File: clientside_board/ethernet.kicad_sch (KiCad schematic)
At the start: 20 parts, among them J3 Ethernet Jack, U2 ENC624J600-I_PT, Y1 25MHz parallel resonant

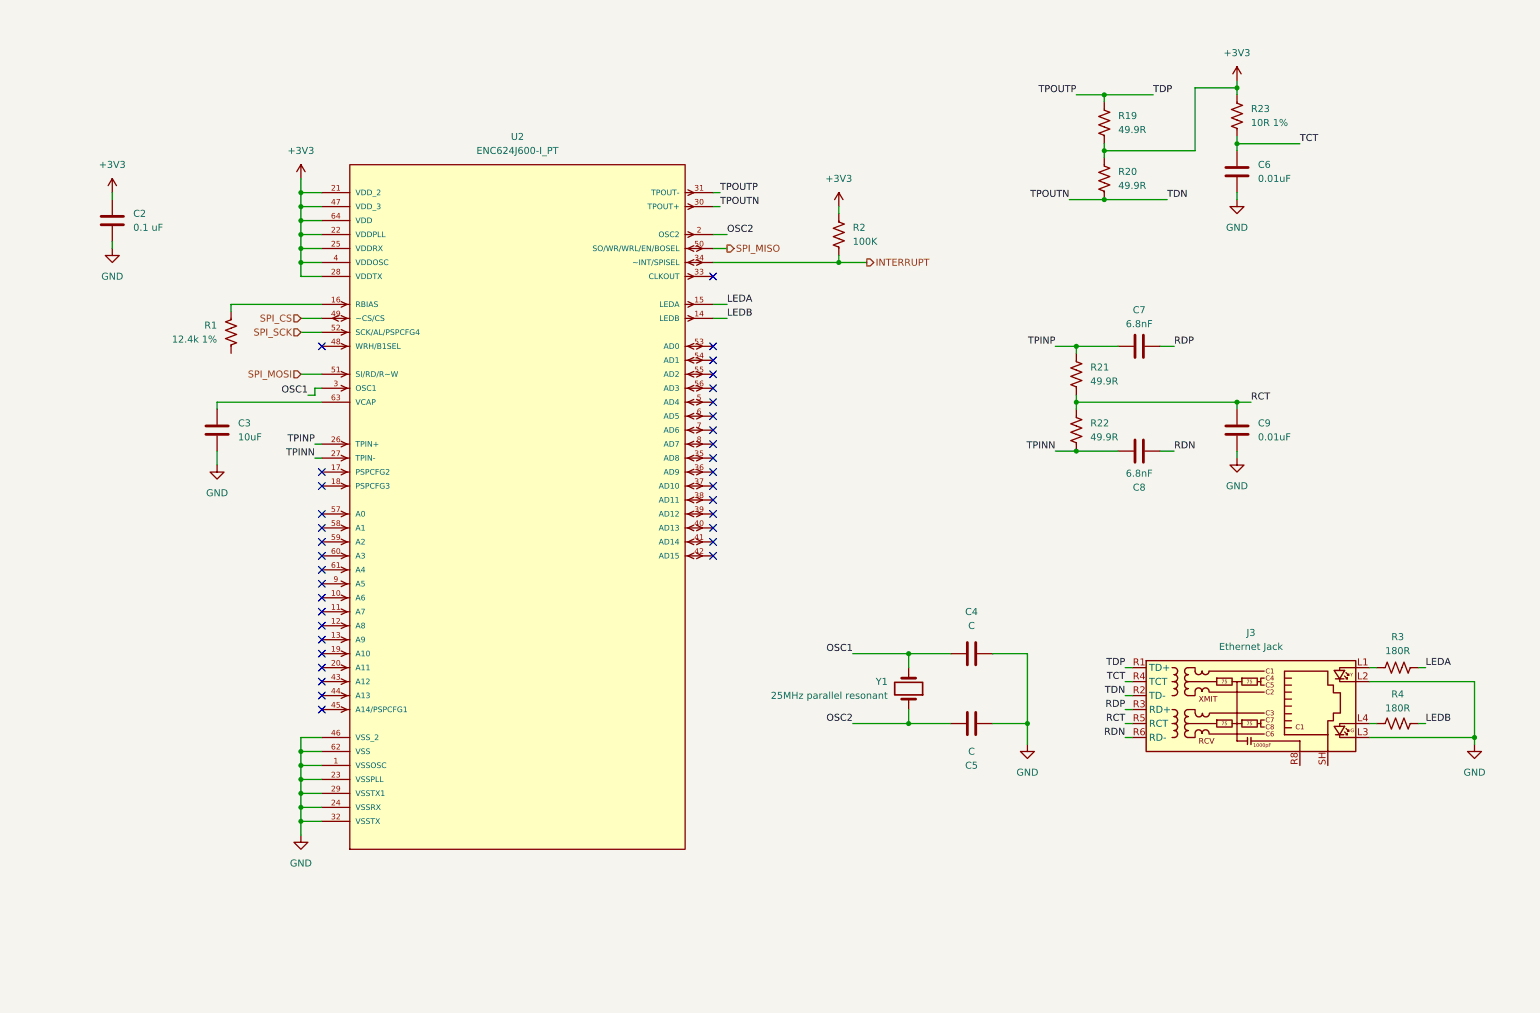
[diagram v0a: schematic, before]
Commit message: Cleanup Power and Ethernet Sheet
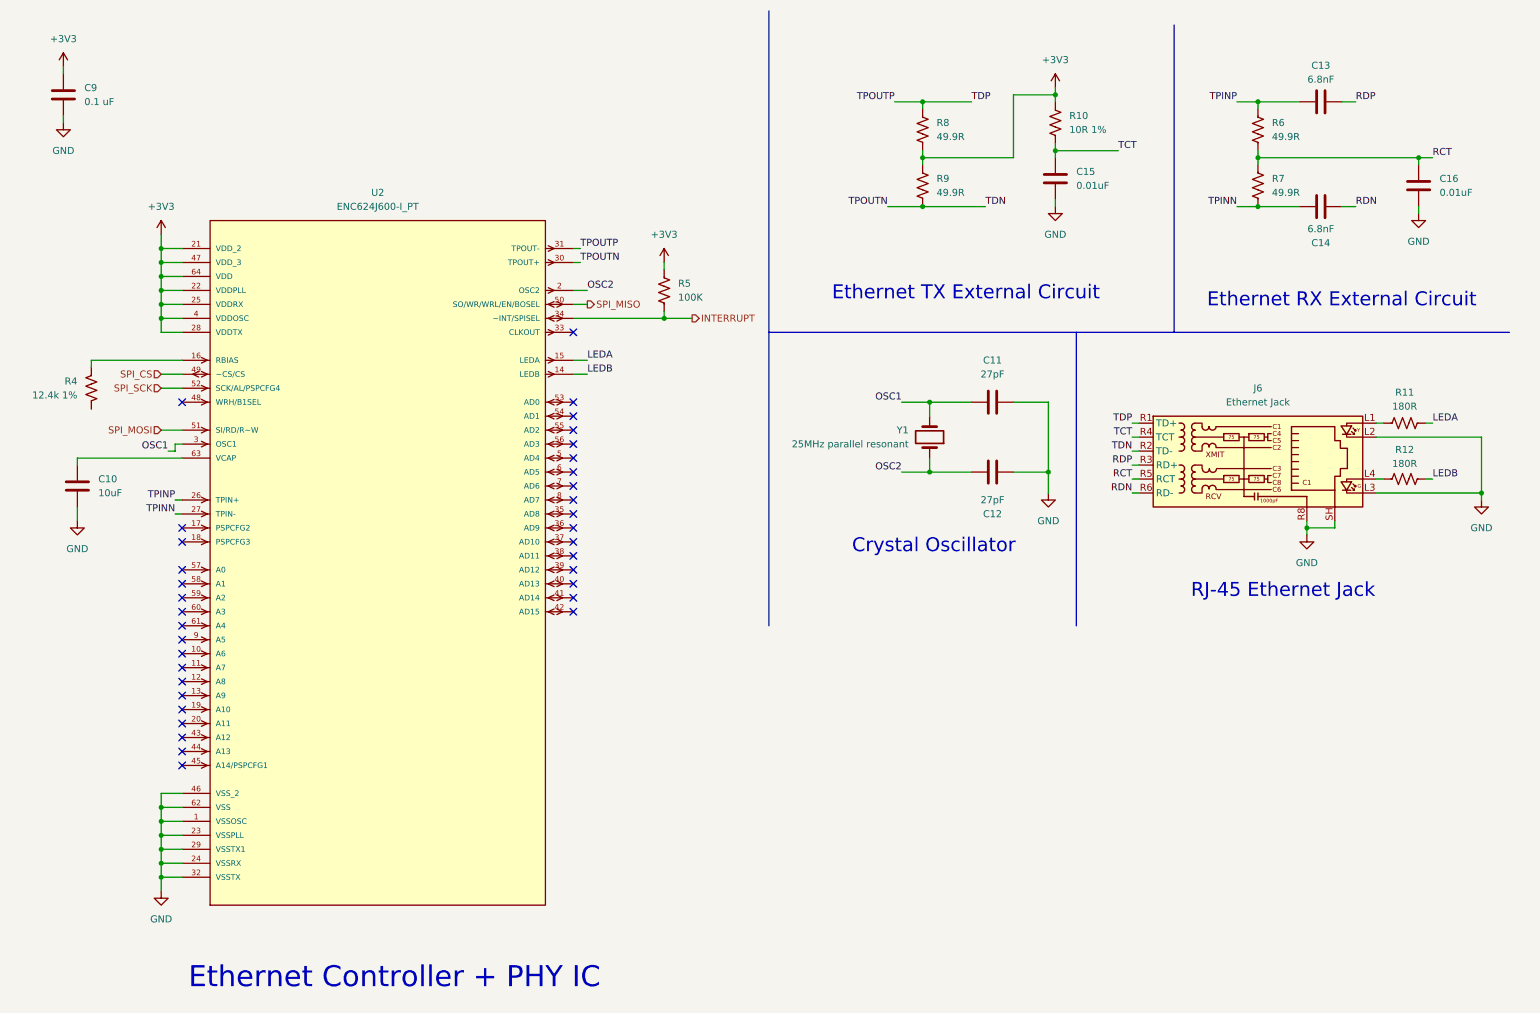
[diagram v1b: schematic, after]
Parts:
- C10: renamed from C3; footprint (none) -> Capacitor_SMD:C_0805_2012Metric_Pad1.18x1.45mm_HandSolder
- C11: renamed from C4; value C -> 27pF; footprint (none) -> Capacitor_SMD:C_0805_2012Metric_Pad1.18x1.45mm_HandSolder
- C12: renamed from C5; value C -> 27pF; footprint (none) -> Capacitor_SMD:C_0805_2012Metric_Pad1.18x1.45mm_HandSolder
- C13: renamed from C7; footprint (none) -> Capacitor_SMD:C_0805_2012Metric_Pad1.18x1.45mm_HandSolder
- C14: renamed from C8; footprint (none) -> Capacitor_SMD:C_0805_2012Metric_Pad1.18x1.45mm_HandSolder
- C15: renamed from C6; footprint (none) -> Capacitor_SMD:C_0805_2012Metric_Pad1.18x1.45mm_HandSolder
- C16: renamed from C9; footprint (none) -> Capacitor_SMD:C_0805_2012Metric_Pad1.18x1.45mm_HandSolder
- C9: renamed from C2; footprint (none) -> Capacitor_SMD:C_0805_2012Metric_Pad1.18x1.45mm_HandSolder
- renumbered J3 to J6, R23 to R10, R3 to R11, R4 to R12, R1 to R4, R2 to R5, R21 to R6, R22 to R7, R19 to R8, R20 to R9
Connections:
- net GND: now also J6.R8, J6.SH
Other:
- note added: "Crystal Oscillator"
- note added: "Ethernet Controller + PHY IC"
- note added: "Ethernet RX External Circuit"
- note added: "Ethernet TX External Circuit"
- note added: "RJ-45 Ethernet Jack"
- title: (none) -> Ethernet connection (Ethernet MAC+PHY and connector)
- moved on the sheet: C10, C11, C12, C13, C14, C15, C16, C9, J6, R10, R11, R12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

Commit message: Start MCU pin connection
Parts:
- renumbered C15 to C13, C13 to C14, C14 to C15, R7 to R10, R8 to R6, R9 to R7, R10 to R8, R6 to R9
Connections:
- net GND: now also R4.2
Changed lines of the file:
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@@
+	(wire
+		(pts
+			(xy 26.67 87.63) (xy 26.67 88.9)
+		)
+		(stroke
+			(width 0)
+			(type default)
+		)
+	)
 	(wire
 		(pts
@@
 		(dnp no)
 		(fields_autoplaced yes)
-		(property "Reference" "C15"
+		(property "Reference" "C13"
 			(at 205.74 44.4499 0)
 			(effects
@@
 			(project ""
 				(path "/94506b77-3097-414f-927c-35c0af27646f/c0b92ac7-0f0f-41de-974e-1086adc34351"
-					(reference "C15")
+					(reference "C13")
 					(unit 1)
 				)
@@
 		(dnp no)
 		(fields_autoplaced yes)
-		(property "Reference" "#PWR046"
+		(property "Reference" "#PWR047"
 			(at 279.4 110.49 0)
 			(effects
@@
 			(project ""
 				(path "/94506b77-3097-414f-927c-35c0af27646f/c0b92ac7-0f0f-41de-974e-1086adc34351"
-					(reference "#PWR046")
+					(reference "#PWR047")
 					(unit 1)
 				)
@@
 		(dnp no)
 		(fields_autoplaced yes)
-		(property "Reference" "#PWR0104"
+		(property "Reference" "#PWR045"
 			(at 247.65 116.84 0)
 			(effects
@@
 			(project ""
 				(path "/94506b77-3097-414f-927c-35c0af27646f/c0b92ac7-0f0f-41de-974e-1086adc34351"
-					(reference "#PWR0104")
+					(reference "#PWR045")
 					(unit 1)
 				)
@@
 		(dnp no)
 		(fields_autoplaced yes)
-		(property "Reference" "R10"
+		(property "Reference" "R8"
 			(at 204.47 34.2899 0)
 			(effects
@@
 			(project ""
 				(path "/94506b77-3097-414f-927c-35c0af27646f/c0b92ac7-0f0f-41de-974e-1086adc34351"
-					(reference "R10")
+					(reference "R8")
+					(unit 1)
+				)
+			)
+		)
+	)
+	(symbol
+		(lib_id "power:GND")
+		(at 26.67 88.9 0)
+		(unit 1)
+		(exclude_from_sim no)
+		(in_bom yes)
+		(on_board yes)
+		(dnp no)
+		(property "Reference" "#PWR0106"
+			(at 26.67 95.25 0)
+			(effects
+				(font
+					(size 1.27 1.27)
+				)
+				(hide yes)
+			)
+		)
+		(property "Value" "GND"
+			(at 26.67 93.218 0)
+			(effects
+				(font
+					(size 1.27 1.27)
+				)
+			)
+		)
+		(property "Footprint" ""
+			(at 26.67 88.9 0)
+			(effects
+				(font
+					(size 1.27 1.27)
+				)
+				(hide yes)
+			)
+		)
+		(property "Datasheet" ""
+			(at 26.67 88.9 0)
+			(effects
+				(font
+					(size 1.27 1.27)
+				)
+				(hide yes)
+			)
+		)
+		(property "Description" "Power symbol creates a global label with name \"GND\" , ground"
+			(at 26.67 88.9 0)
+			(effects
+				(font
+					(size 1.27 1.27)
+				)
+				(hide yes)
+			)
+		)
+		(pin "1"
+		)
+		(instances
+			(project ""
+				(path "/94506b77-3097-414f-927c-35c0af27646f/c0b92ac7-0f0f-41de-974e-1086adc34351"
+					(reference "#PWR0106")
 					(unit 1)
 				)
@@
 		(dnp no)
 		(fields_autoplaced yes)
-		(property "Reference" "R8"
+		(property "Reference" "R6"
 			(at 180.34 35.5599 0)
 			(effects
@@
 			(project ""
 				(path "/94506b77-3097-414f-927c-35c0af27646f/c0b92ac7-0f0f-41de-974e-1086adc34351"
-					(reference "R8")
+					(reference "R6")
 					(unit 1)
 				)
@@
 		(on_board yes)
 		(dnp no)
-		(property "Reference" "C14"
+		(property "Reference" "C15"
 			(at 250.19 57.404 90)
 			(effects
@@
 			(project "clientside_board"
 				(path "/94506b77-3097-414f-927c-35c0af27646f/c0b92ac7-0f0f-41de-974e-1086adc34351"
-					(reference "C14")
+					(reference "C15")
 					(unit 1)
 				)
@@
 		(dnp no)
 		(fields_autoplaced yes)
-		(property "Reference" "R6"
+		(property "Reference" "R9"
 			(at 241.3 35.5599 0)
 			(effects
@@
 			(project "clientside_board"
 				(path "/94506b77-3097-414f-927c-35c0af27646f/c0b92ac7-0f0f-41de-974e-1086adc34351"
-					(reference "R6")
+					(reference "R9")
 					(unit 1)
 				)
@@
 		(dnp no)
 		(fields_autoplaced yes)
-		(property "Reference" "#PWR045"
+		(property "Reference" "#PWR046"
 			(at 267.97 58.42 0)
 			(effects
@@
 			(project ""
 				(path "/94506b77-3097-414f-927c-35c0af27646f/c0b92ac7-0f0f-41de-974e-1086adc34351"
-					(reference "#PWR045")
+					(reference "#PWR046")
 					(unit 1)
 				)
@@
 		(on_board yes)
 		(dnp no)
-		(property "Reference" "C13"
+		(property "Reference" "C14"
 			(at 250.19 25.146 90)
 			(effects
@@
 			(project ""
 				(path "/94506b77-3097-414f-927c-35c0af27646f/c0b92ac7-0f0f-41de-974e-1086adc34351"
-					(reference "C13")
+					(reference "C14")
 					(unit 1)
 				)
@@
 		(dnp no)
 		(fields_autoplaced yes)
-		(property "Reference" "R7"
+		(property "Reference" "R10"
 			(at 241.3 45.7199 0)
 			(effects
@@
 			(project "clientside_board"
 				(path "/94506b77-3097-414f-927c-35c0af27646f/c0b92ac7-0f0f-41de-974e-1086adc34351"
-					(reference "R7")
+					(reference "R10")
 					(unit 1)
 				)
@@
 		(dnp no)
 		(fields_autoplaced yes)
-		(property "Reference" "R9"
+		(property "Reference" "R7"
 			(at 180.34 45.7199 0)
 			(effects
@@
 			(project "clientside_board"
 				(path "/94506b77-3097-414f-927c-35c0af27646f/c0b92ac7-0f0f-41de-974e-1086adc34351"
-					(reference "R9")
-					(unit 1)
-				)
+					(reference "R7")
+					(unit 1)
+				)

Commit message: Fix decoupling cap
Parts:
- removed Y1: 25MHz parallel resonant, symbol Device:Crystal
- added C13, C14, C15, C16: 0.1 uF, Capacitor_SMD:C_0805_2012Metric_Pad1.18x1.45mm_HandSolder, symbol Device:C
- added TP1: ETH_SPI_SCK, symbol Connector:TestPoint
- added TP2: ETH_SPI_CS, symbol Connector:TestPoint
- added TP3: ETH_SPI_MOSI, symbol Connector:TestPoint
- added TP4: ETH_SPI_MISO, symbol Connector:TestPoint
- added Y1: ECS-2520MV-250-BN, Oscillator:Oscillator_SMD_ECS_2520MV-xxx-xx-4Pin_2.5x2.0mm, symbol Oscillator:ECS-2520MV-xxx-xx
- C11, C12: value 27pF -> 0.1 uF
- R6, R7: value 49.9R -> 49.9R 1%
- renumbered C13 to C17, C14 to C18, C15 to C19, C16 to C20
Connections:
- net +3V3: now also C11.1, C12.1, C13.1, C14.1, C15.1, C16.1, Y1.4 (VDD)
- net GND: now also C13.2, C14.2, C15.2, C16.2, Y1.2 (GND)
- net OSC1: now also Y1.3 (OUT); no longer C11.1
- net SPI_CS: now also TP2.1
- net SPI_MISO: now also TP4.1
- net SPI_MOSI: now also TP3.1
- net SPI_SCK: now also TP1.1
- net OSC2: no longer names the net of U2.2 (OSC2)
- net OSC2: no longer C12.1
- no-connect marks 35 -> 37
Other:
- note added: "Decoupling Capacitors"
- note added: "Testpoints"
- moved on the sheet: C10, C9, R4, R5, U2

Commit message: Top sheet update
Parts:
- added R6: 100K DNP, Resistor_SMD:R_0805_2012Metric_Pad1.20x1.40mm_HandSolder, symbol Device:R_US
- C10: renamed from C9; footprint Capacitor_SMD:C_0805_2012Metric_Pad1.18x1.45mm_HandSolder -> Capacitor_SMD:C_0603_1608Metric_Pad1.08x0.95mm_HandSolder
- C11, C12, C13, C14, C15, C16, C17, C18, C19, C20: footprint Capacitor_SMD:C_0805_2012Metric_Pad1.18x1.45mm_HandSolder -> Capacitor_SMD:C_0603_1608Metric_Pad1.08x0.95mm_HandSolder
- C9: renamed from C10; footprint Capacitor_SMD:C_0805_2012Metric_Pad1.18x1.45mm_HandSolder -> Capacitor_SMD:C_0603_1608Metric_Pad1.08x0.95mm_HandSolder
- R5: value 100K -> 100K DNP
- renumbered R9 to R10, R10 to R11, R11 to R12, R12 to R13, R6 to R7, R7 to R8, R8 to R9
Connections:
- net GND: now also R6.2
- net INTERRUPT: now also R6.1
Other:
- note added: "Populate only when SPI interface is used"
- note added: "Populate only when parallel interface is used"
- moved on the sheet: R5
